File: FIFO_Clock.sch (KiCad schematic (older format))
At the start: 50 parts, among them J1 U262-16XN-4BVC11, J2 AVR-ISP-6, SW1 SKHMQKE010, SW2 SW_5_Way, U1 ATtiny84A-SSUR, U2 DS1307Z+, Y1 32.768 kHz

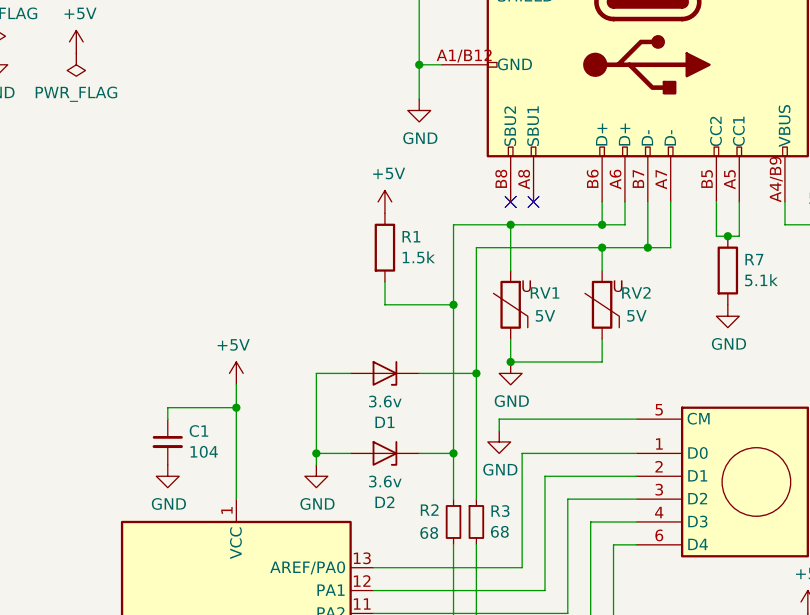
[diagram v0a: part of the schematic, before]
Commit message: v1.1 changes transferred, FILO->FIFO change
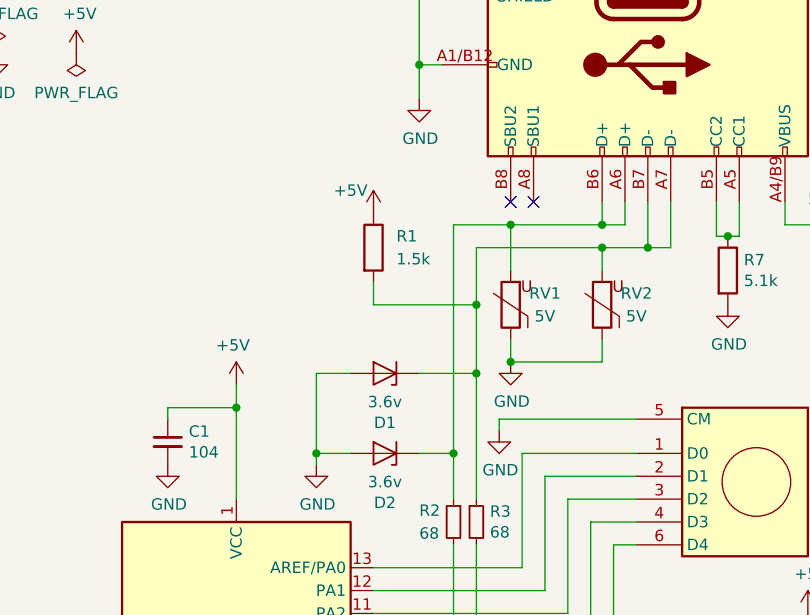
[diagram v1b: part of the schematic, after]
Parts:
- C2: footprint Capacitor_SMD:C_0603_1608Metric_Pad1.05x0.95mm_HandSolder -> Capacitor_SMD:CP_Elec_6.3x5.8
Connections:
- net at D2.1 (K), J1.A6 (D+), J1.B6 (D+)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: no longer R1.2
- net at D1.1 (K), J1.A7 (D-), J1.B7 (D-)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: now also R1.2
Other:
- moved on the sheet: R1
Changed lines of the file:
@@
 Wire Wire Line
 	3700 1850 3700 1750
-Wire Wire Line
-	3050 1850 3050 2200
 Connection ~ 3700 1850
 Wire Wire Line
-	3150 1950 3150 2500
+	3150 1950 3150 2200
 Wire Wire Line
 	4000 1750 4000 1950
@@
 F 0 "C2" H 5218 2096 50  0000 L CNN
 F 1 "226" H 5218 2005 50  0000 L CNN
-F 2 "Capacitor_SMD:C_0603_1608Metric_Pad1.05x0.95mm_HandSolder" H 5138 1900 50  0001 C CNN
+F 2 "Capacitor_SMD:CP_Elec_6.3x5.8" H 5138 1900 50  0001 C CNN
 F 3 "~" H 5100 2050 50  0001 C CNN
 	1    5100 2050
@@
 L power:+5V #PWR09
 U 1 1 5CB1C05D
-P 2750 1800
-F 0 "#PWR09" H 2750 1650 50  0001 C CNN
-F 1 "+5V" H 2765 1973 50  0000 C CNN
-F 2 "" H 2750 1800 50  0001 C CNN
-F 3 "" H 2750 1800 50  0001 C CNN
-	1    2750 1800
+P 2700 1800
+F 0 "#PWR09" H 2700 1650 50  0001 C CNN
+F 1 "+5V" H 2600 1900 50  0000 C CNN
+F 2 "" H 2700 1800 50  0001 C CNN
+F 3 "" H 2700 1800 50  0001 C CNN
+	1    2700 1800
 	1    0    0    -1
 $EndComp
@@
 L Device:R R1
 U 1 1 5CB27277
-P 2750 1950
-F 0 "R1" H 2820 1996 50  0000 L CNN
-F 1 "1.5k" H 2820 1905 50  0000 L CNN
-F 2 "Resistor_SMD:R_0603_1608Metric_Pad1.05x0.95mm_HandSolder" V 2680 1950 50  0001 C CNN
-F 3 "~" H 2750 1950 50  0001 C CNN
-	1    2750 1950
-	1    0    0    -1
-$EndComp
-Wire Wire Line
-	2750 2100 2750 2200
-Wire Wire Line
-	2750 2200 3050 2200
-Connection ~ 3050 2200
-Wire Wire Line
-	3050 2200 3050 2850
+P 2700 1950
+F 0 "R1" H 2800 2000 50  0000 L CNN
+F 1 "1.5k" H 2800 1900 50  0000 L CNN
+F 2 "Resistor_SMD:R_0603_1608Metric_Pad1.05x0.95mm_HandSolder" V 2630 1950 50  0001 C CNN
+F 3 "~" H 2700 1950 50  0001 C CNN
+	1    2700 1950
+	1    0    0    -1
+$EndComp
 Wire Wire Line
 	3150 2500 2900 2500
@@
 	1    0    0    -1
 $EndComp
-Wire Wire Line
-	3150 3250 3150 4350
 $Comp
 L Device:R_Small R2
@@
 	-1   0    0    -1
 $EndComp
+Wire Wire Line
+	3050 1850 3050 2850
+Wire Wire Line
+	3150 3250 3150 4350
+Wire Wire Line
+	2700 2200 3150 2200
+Connection ~ 3150 2200
+Wire Wire Line
+	3150 2200 3150 2500
+Wire Wire Line
+	2700 2100 2700 2200
 $EndSCHEMATC

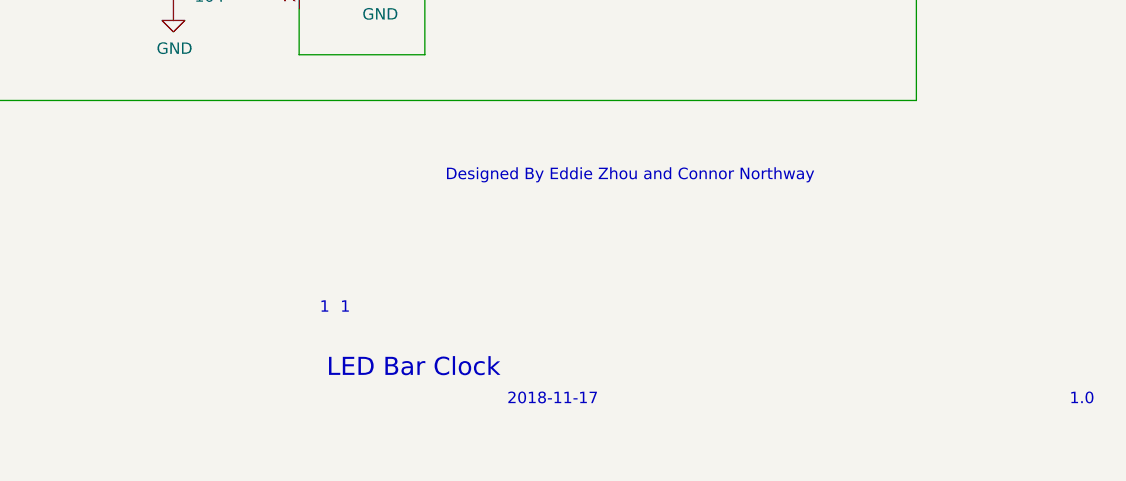
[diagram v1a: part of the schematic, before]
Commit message: change schematic to US letter, add image to README
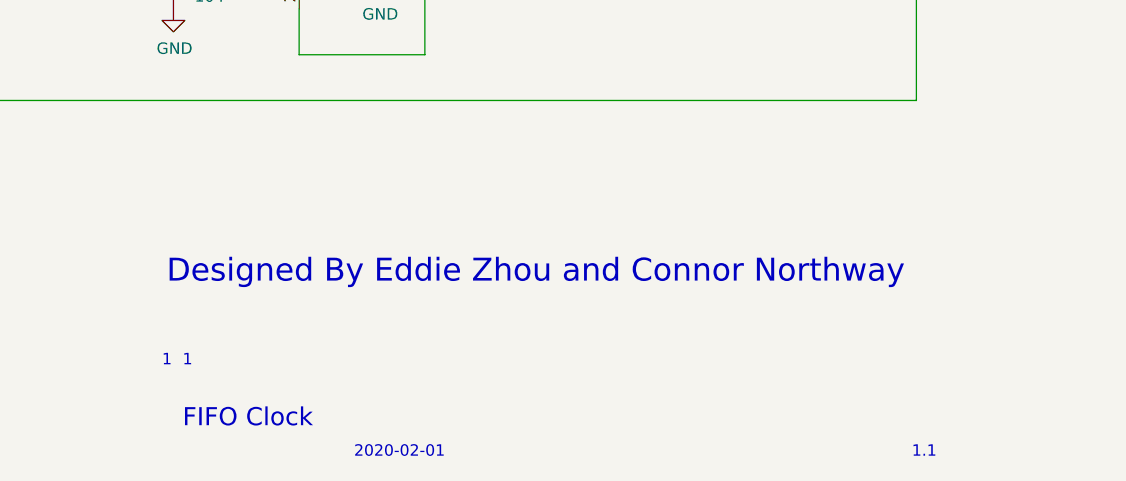
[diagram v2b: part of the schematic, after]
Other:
- note added: "1.1"
- note added: "2020-02-01"
- note added: "FIFO Clock"
- note removed: "1.0"
- note removed: "2018-11-17"
- note removed: "LED Bar Clock"
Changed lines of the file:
@@
 EESchema Schematic File Version 4
-LIBS:LED_Bar_Clock-cache
-EELAYER 29 0
+LIBS:FIFO_Clock-cache
+EELAYER 30 0
 EELAYER END
-$Descr A4 11693 8268
+$Descr USLetter 11000 8500
 encoding utf-8
 Sheet 1 1
@@
 	0    -1   -1   0
 $EndComp
-Text Notes 7320 7520 0    79   ~ 0
-LED Bar Clock
-Text Notes 10570 7640 0    50   ~ 0
-1.0
-Text Notes 7290 7240 0    50   ~ 0
+Text Notes 6690 7740 0    79   ~ 0
+FIFO Clock
+Text Notes 9880 7870 0    50   ~ 0
+1.1
+Text Notes 6690 7470 0    50   ~ 0
 1
-Text Notes 7380 7240 0    50   ~ 0
-1
-Text Notes 8110 7640 0    50   ~ 0
-2018-11-17
-Text Notes 7840 6660 0    50   ~ 0
+Text Notes 7440 7870 0    50   ~ 0
+2020-02-01
+Text Notes 6620 7110 0    100  ~ 0
 Designed By Eddie Zhou and Connor Northway
 $Comp
@@
 Wire Wire Line
 	2700 2100 2700 2200
+Text Notes 6600 7470 0    50   ~ 0
+1
 $EndSCHEMATC
